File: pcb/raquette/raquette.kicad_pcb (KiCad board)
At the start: 2 copper layers, 80 x 120 mm, 12 parts, among them U1 Teensy 4.1

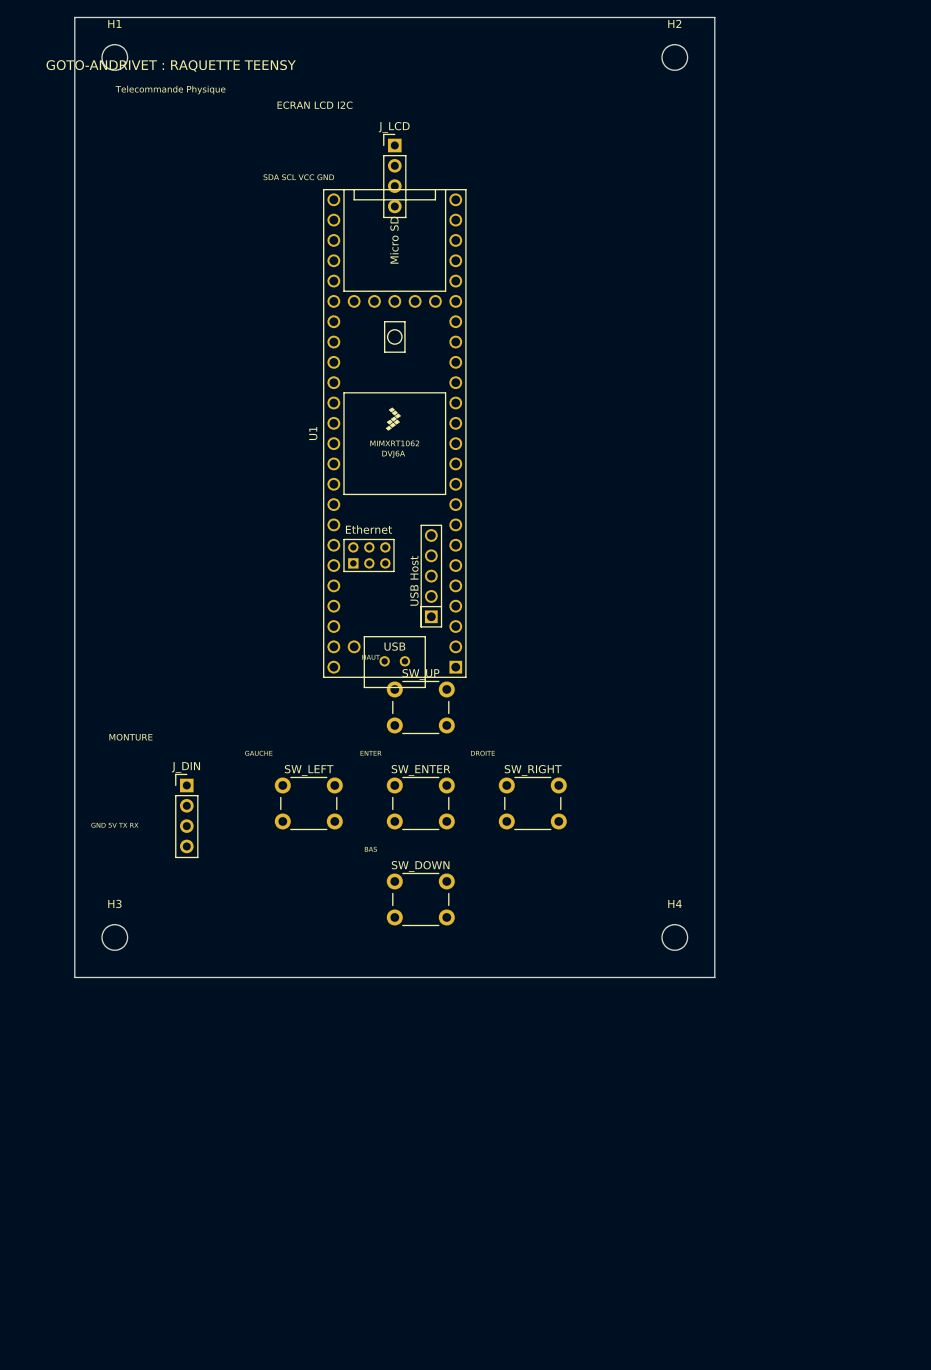
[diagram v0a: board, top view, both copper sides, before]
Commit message: feat(pcb): integration physique de l'ecran LCD 2004/1602 avec entretoises M3 sur le PCB de la raquette
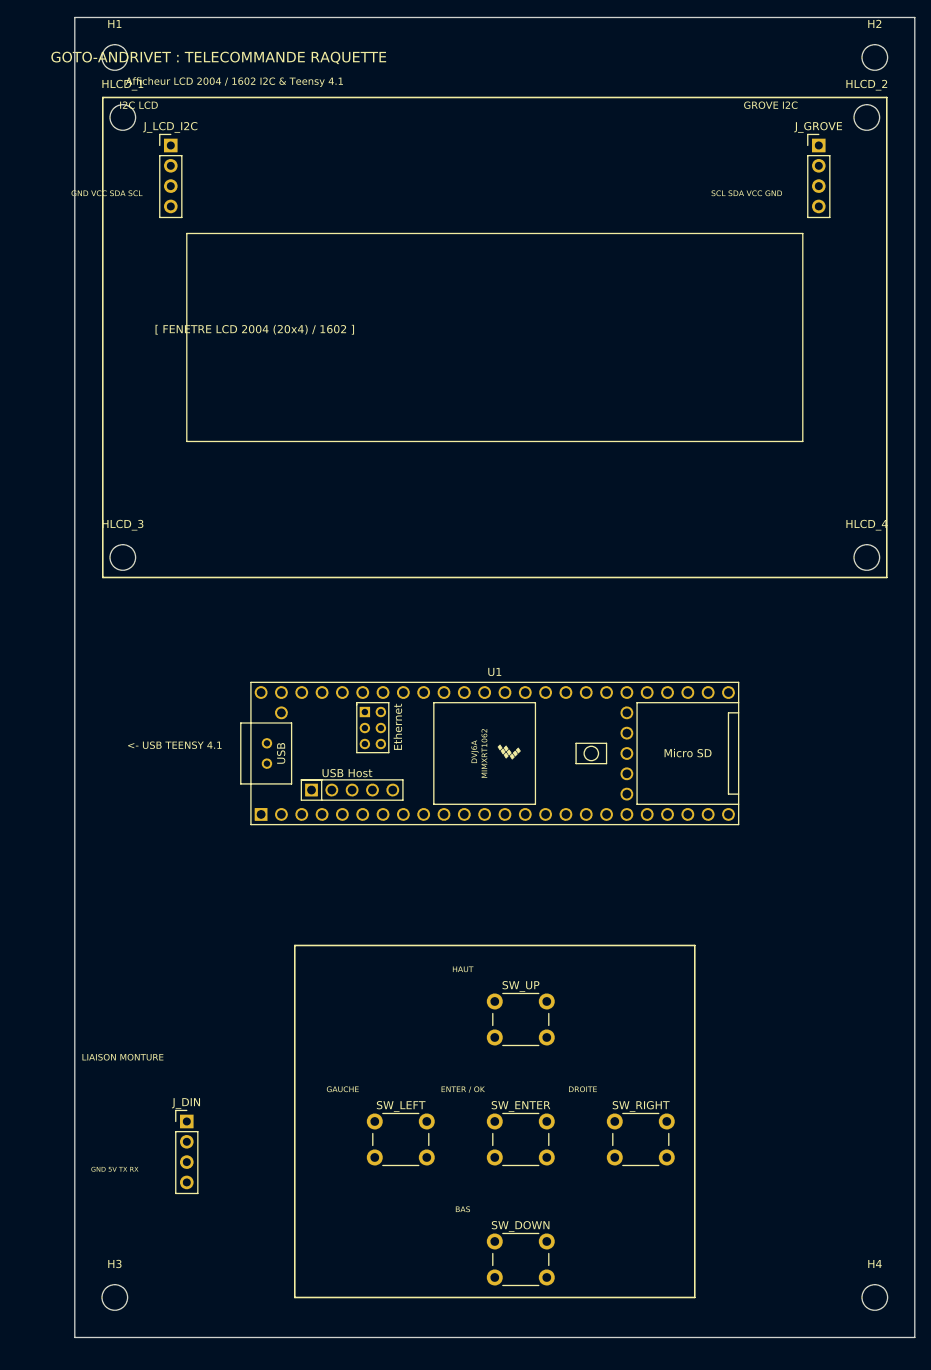
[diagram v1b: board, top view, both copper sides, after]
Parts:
- removed J_LCD: LCD Grove I2C, PinHeader_1x04_P2.54mm_Vertical
- added HLCD_1: M3 Entretoise LCD, MountingHole_3.2mm_M3, F.Cu at (6.00, 12.5)
- added HLCD_2: M3 Entretoise LCD, MountingHole_3.2mm_M3, F.Cu at (99.0, 12.5)
- added HLCD_3: M3 Entretoise LCD, MountingHole_3.2mm_M3, F.Cu at (6.00, 67.5)
- added HLCD_4: M3 Entretoise LCD, MountingHole_3.2mm_M3, F.Cu at (99.0, 67.5)
- added J_GROVE: Grove I2C Aux, PinHeader_1x04_P2.54mm_Vertical, F.Cu at (93.0, 16.0)
- added J_LCD_I2C: LCD Backpack I2C, PinHeader_1x04_P2.54mm_Vertical, F.Cu at (12.0, 16.0)
- H1, H2, H3, H4: value M3 -> Fixation Boitier M3
- SW_ENTER: value ENTER -> ENTER / OK
- moved H4 51.5 mm to (100.0, 160.0)
- moved SW_DOWN 46.7 mm to (52.5, 153.0)
- moved H3 45.0 mm to (5.00, 160.0)
- moved SW_RIGHT 44.1 mm to (67.5, 138.0)
- moved SW_ENTER 43.8 mm to (52.5, 138.0)
- moved SW_LEFT 43.5 mm to (37.5, 138.0)
- moved J_DIN 42.0 mm to (14.0, 138.0)
- moved U1 41.9 mm to (52.5, 92.0), turned to 0 degrees
- moved SW_UP 41.0 mm to (52.5, 123.0)
- moved H2 25.0 mm to (100.0, 5.00)
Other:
- board size 80 x 120 mm -> 105 x 165 mm
- board text added: "<- USB TEENSY 4.1"
- board text added: "Afficheur LCD 2004 / 1602 I2C & Teensy 4.1"
- board text added: "ENTER / OK"
- board text added: "GND VCC SDA SCL"
- board text added: "GOTO-ANDRIVET : TELECOMMANDE RAQUETTE"
- board text added: "GROVE I2C"
- board text added: "I2C LCD"
- board text added: "LIAISON MONTURE"
- board text added: "SCL SDA VCC GND"
- board text added: "[ FENETRE LCD 2004 (20x4) / 1602 ]"
- board text removed: "ECRAN LCD I2C"
- board text removed: "ENTER"
- board text removed: "GOTO-ANDRIVET : RAQUETTE TEENSY"
- board text removed: "MONTURE"
- board text removed: "SDA SCL VCC GND"
- board text removed: "Telecommande Physique"

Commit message: feat(pcb): passage en 36V haute puissance, integration de 4 drivers 4A TMC5160, convertisseur buck 36V->5V et borniers directs moteurs
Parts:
- H1, H2, H3, H4: value Fixation Boitier M3 -> M3 Fixation

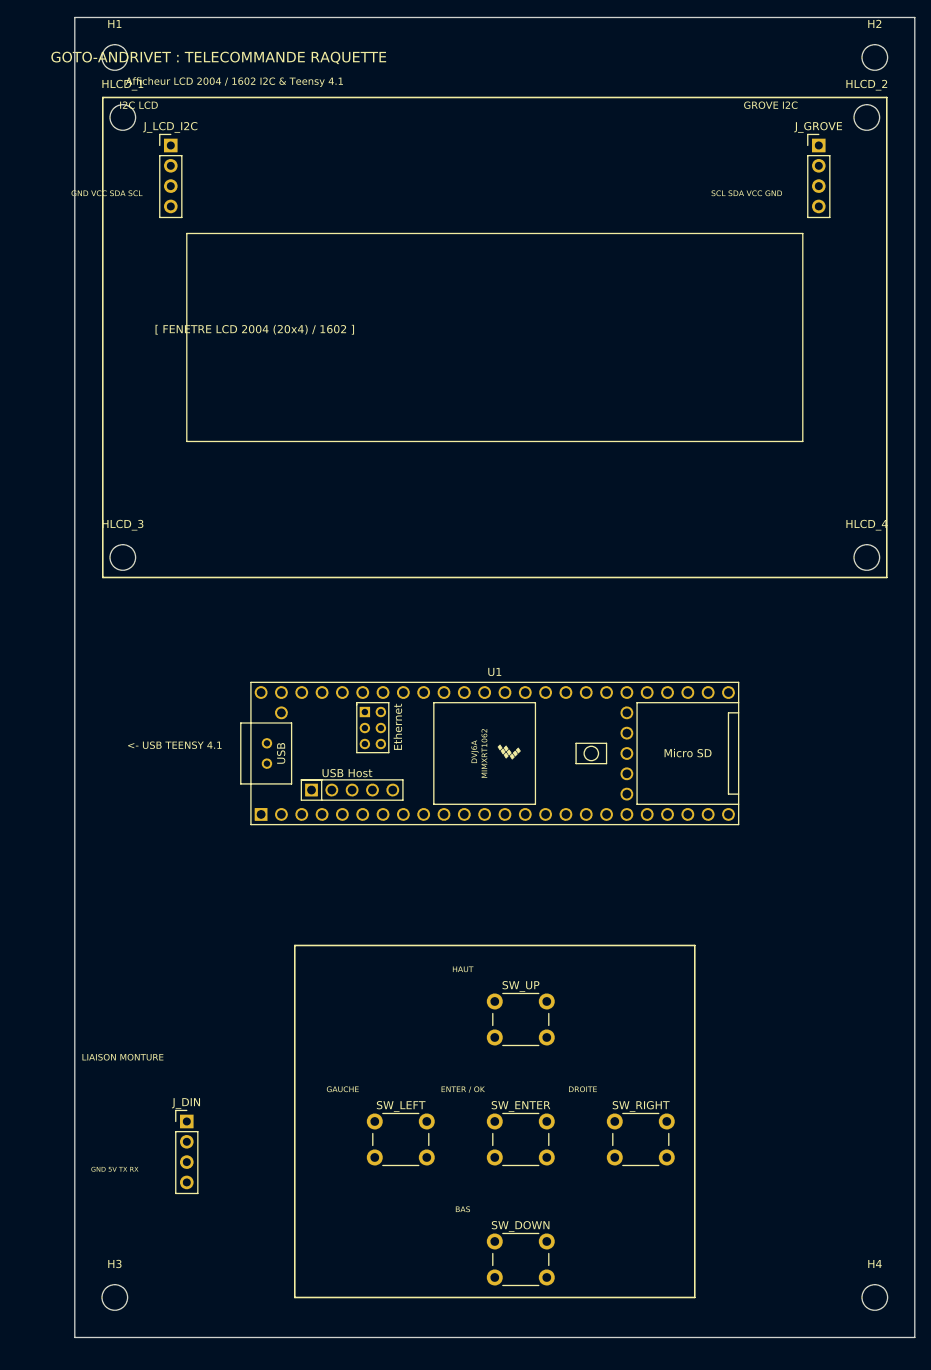
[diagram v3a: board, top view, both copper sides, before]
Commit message: feat(pcb): orientation de tous les connecteurs et borniers vers l exterieur du PCB
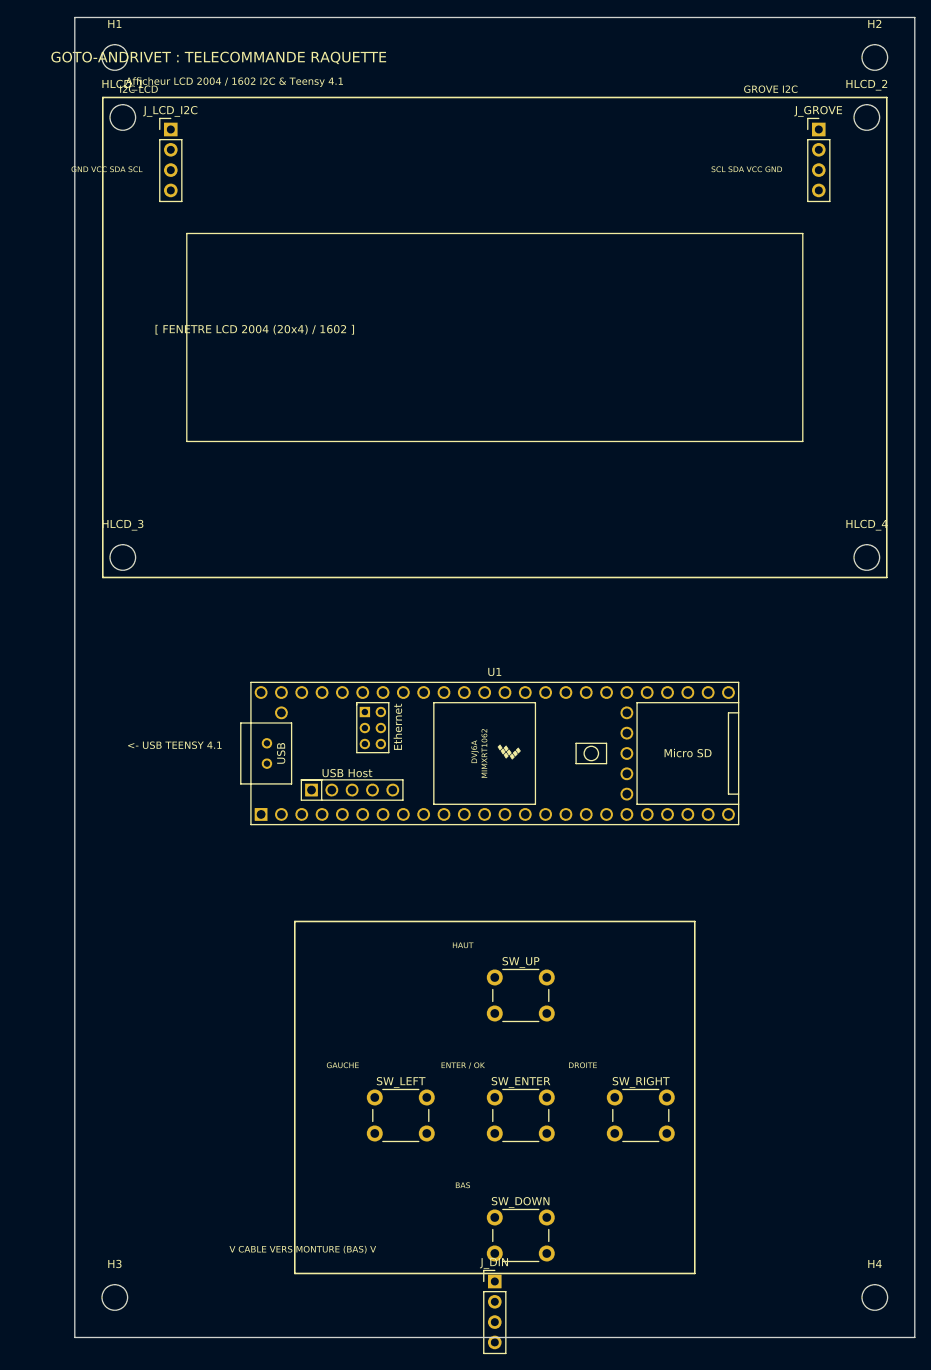
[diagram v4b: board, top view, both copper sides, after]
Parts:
- moved J_DIN 43.4 mm to (52.5, 158.0)
- moved SW_DOWN 3.00 mm to (52.5, 150.0)
- moved SW_ENTER 3.00 mm to (52.5, 135.0)
- moved SW_LEFT 3.00 mm to (37.5, 135.0)
- moved SW_RIGHT 3.00 mm to (67.5, 135.0)
- moved SW_UP 3.00 mm to (52.5, 120.0)
- moved J_GROVE 2.00 mm to (93.0, 14.0)
- moved J_LCD_I2C 2.00 mm to (12.0, 14.0)
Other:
- board text added: "V CABLE VERS MONTURE (BAS) V"
- board text removed: "GND 5V TX RX"
- board text removed: "LIAISON MONTURE"
